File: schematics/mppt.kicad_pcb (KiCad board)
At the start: 2 copper layers, 85.7 x 58.9 mm, 164 parts, among them J1 nokia5110, J2 UART, J3 SWD, J4 buck/boost, J5 HV+, J6 HV-, J7 LV+, J8 LV-, Q1 Q_NMOS_GDS, Q2 Q_NMOS_GDS, SW1 push, SW2 push, SW3 push, SW4 push, SW5 push, U1 LMR16006XDDCR, U2 LMR16006XDDCR, U3 STM32F103C8Tx, U4 INA199, U5 lm5109, U6 INA199

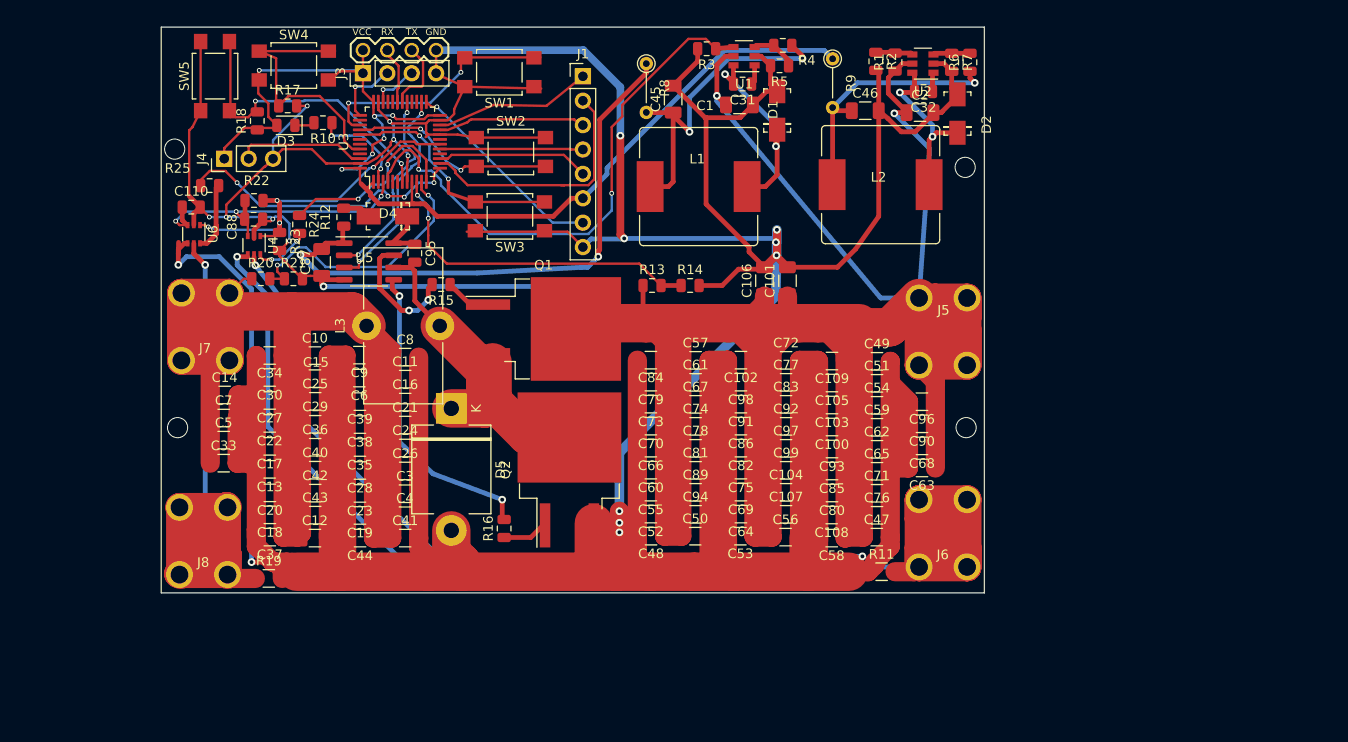
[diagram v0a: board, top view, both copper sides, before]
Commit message: update schematic
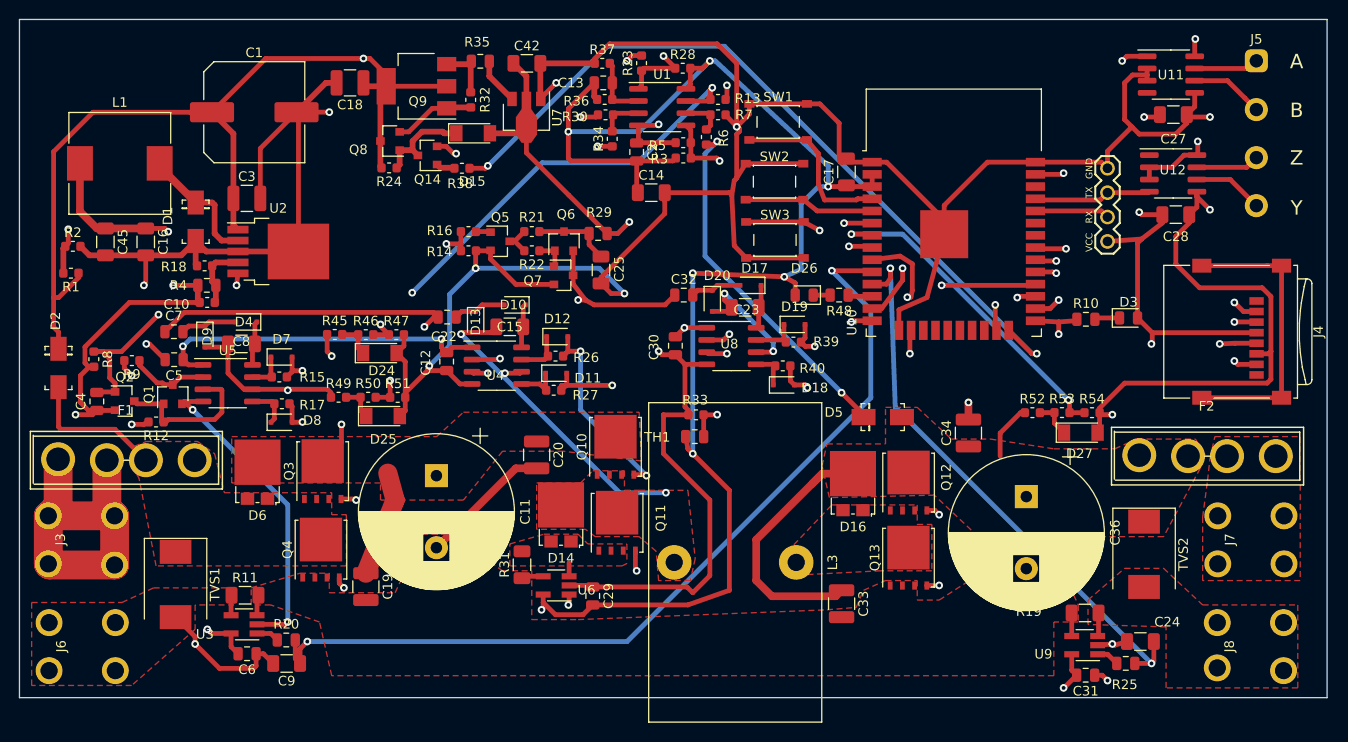
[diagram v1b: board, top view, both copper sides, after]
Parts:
- removed C100, C101, C102, C103, C104, C105, C106, C107, C108, C109, C21, C26, C35, C37, C38, C39, C40, C41, C43, C44, C46, C47, C48, C49, C50, C51, C52, C53, C54, C55, C56, C57, C58, C59, C60, C61, C62, C63, C64, C65, C66, C67, C68, C69, C70, C71, C72, C73, C74, C75, C76, C77, C78, C79, C80, C81, C82, C83, C84, C85, C86, C87, C89, C90, C91, C92, C93, C94, C96, C97, C98, C99: 10uF, Capacitor_SMD:C_1206_3216Metric
- removed C110, C88: .22uF, Capacitor_SMD:C_0805_2012Metric
- removed C95: 1uF, Capacitor_SMD:C_0805_2012Metric
- removed J1: nokia5110, Connector_PinHeader_2.54mm:PinHeader_1x08_P2.54mm_Vertical
- removed L2: 10uH, Inductor_SMD:L_Bourns_SRR1210A
- removed SW4, SW5: push, Button_Switch_SMD:SW_SPST_TL3305A
- added D10: D, Diode_SMD:D_SOD-323F, F.Cu at (149.1, 105.9)
- added D11: D, Diode_SMD:D_SOD-323F, F.Cu at (153.4, 113.0)
- added D12: D, Diode_SMD:D_SOD-323F, F.Cu at (153.5, 109.2)
- added D13: D, Diode_SMD:D_SOD-323F, F.Cu at (145.0, 107.7)
- added D14: D_Schottky_AAK, Package_TO_SOT_SMD:TO-277A, F.Cu at (153.9, 127.8)
- added D15: 5.6v, Diode_SMD:D_MiniMELF, F.Cu at (144.8, 88.1)
- added D16: D_Schottky_AAK, Package_TO_SOT_SMD:TO-277A, F.Cu at (184.3, 124.5)
- added D17: D, Diode_SMD:D_SOD-323F, F.Cu at (173.7, 103.9)
- added D18: D, Diode_SMD:D_SOD-323F, F.Cu at (177.1, 114.3)
- added D19: D, Diode_SMD:D_SOD-323F, F.Cu at (178.2, 108.0)
- added D20: D, Diode_SMD:D_SOD-323F, F.Cu at (169.7, 105.5)
- added D24: 5.6v, Diode_SMD:D_MiniMELF, F.Cu at (135.1, 110.9)
- added D25: 5.6v, Diode_SMD:D_MiniMELF, F.Cu at (135.4, 117.5)
- added D26: YELLOW, LED_SMD:LED_0805_2012Metric, F.Cu at (179.2, 104.9)
- added D27: 5.6v, Diode_SMD:D_MiniMELF, F.Cu at (208.0, 119.2)
- added D6: D_Schottky_AAK, Package_TO_SOT_SMD:TO-277A, F.Cu at (122.3, 123.3)
- added D7: D, Diode_SMD:D_SOD-323F, F.Cu at (124.8, 111.3)
- added D8: D, Diode_SMD:D_SOD-323F, F.Cu at (124.8, 118.1)
- added D9: D, Diode_SMD:D_SOD-323F, F.Cu at (116.8, 109.2)
- added F1: FUSE, mppt_footprints:BladeFuse-CarType, F.Cu at (108.7, 122.1)
- added F2: FUSE, mppt_footprints:BladeFuse-CarType, F.Cu at (221.2, 121.7)
- added Q10: Q_NMOS_GDS, mppt_footprints:TDSON-8-1, F.Cu at (159.6, 120.7)
- added Q11: Q_NMOS_GDS, mppt_footprints:TDSON-8-1, F.Cu at (159.8, 128.6)
- added Q12: Q_NMOS_GDS, mppt_footprints:TDSON-8-1, F.Cu at (190.1, 124.4)
- added Q13: Q_NMOS_GDS, mppt_footprints:TDSON-8-1, F.Cu at (190.1, 132.2)
- added Q14: Q_NPN_BEC, Package_TO_SOT_SMD:SOT-23, F.Cu at (140.0, 90.4)
- added Q3: Q_NMOS_GDS, mppt_footprints:TDSON-8-1, F.Cu at (129.1, 123.2)
- added Q4: Q_NMOS_GDS, mppt_footprints:TDSON-8-1, F.Cu at (128.9, 131.4)
- added Q5: Q_NPN_BEC, Package_TO_SOT_SMD:SOT-23, F.Cu at (147.6, 99.3)
- added Q6: Q_NPN_BEC, Package_TO_SOT_SMD:SOT-23, F.Cu at (154.2, 99.3)
- added Q7: Q_PNP_BCE, Package_TO_SOT_SMD:SOT-23, F.Cu at (154.2, 102.8)
- added Q8: Q_NPN_BEC, Package_TO_SOT_SMD:SOT-23, F.Cu at (136.1, 88.9)
- added Q9: BCP56, Package_TO_SOT_SMD:SOT-223-3_TabPin2, F.Cu at (138.9, 83.2)
- added R26: 33, Resistor_SMD:R_0603_1608Metric, F.Cu at (153.3, 111.3)
- added R27: 33, Resistor_SMD:R_0603_1608Metric, F.Cu at (153.2, 114.8)
- added R28: 10k, Resistor_SMD:R_0603_1608Metric, F.Cu at (166.6, 81.3)
- added R29: 10, Resistor_SMD:R_0805_2012Metric, F.Cu at (157.8, 98.5)
- added R30: 100k, Resistor_SMD:R_0603_1608Metric, F.Cu at (158.6, 86.1)
- added R31: .001, Resistor_SMD:R_1206_3216Metric, F.Cu at (149.9, 133.0)
- added R32: 1k, Resistor_SMD:R_0603_1608Metric, F.Cu at (144.5, 84.6)
- added R33: 10k, Resistor_SMD:R_0603_1608Metric, F.Cu at (168.0, 117.4)
- added R34: 1k, Resistor_SMD:R_0603_1608Metric, F.Cu at (159.3, 88.6)
- added R35: 10, Resistor_SMD:R_0805_2012Metric, F.Cu at (145.5, 80.6)
- added R36: 100k, Resistor_SMD:R_0603_1608Metric, F.Cu at (158.5, 84.5)
- added R37: 10k, Resistor_SMD:R_0603_1608Metric, F.Cu at (158.2, 80.8)
- added R38: 100k, Resistor_SMD:R_0603_1608Metric, F.Cu at (143.6, 91.7)
- added R39: 33, Resistor_SMD:R_0603_1608Metric, F.Cu at (178.1, 109.8)
- added R40: 33, Resistor_SMD:R_0603_1608Metric, F.Cu at (177.0, 112.3)
- added R45: 333k, Resistor_SMD:R_0603_1608Metric, F.Cu at (130.4, 109.0)
- added R46: 10k, Resistor_SMD:R_0603_1608Metric, F.Cu at (133.6, 109.0)
- added R47: 10k, Resistor_SMD:R_0603_1608Metric, F.Cu at (136.8, 109.0)
- added R48: 510, Resistor_SMD:R_0805_2012Metric, F.Cu at (182.9, 104.9)
- added R49: 333k, Resistor_SMD:R_0603_1608Metric, F.Cu at (130.8, 115.5)
- added R50: 10k, Resistor_SMD:R_0603_1608Metric, F.Cu at (133.8, 115.5)
- added R51: 10k, Resistor_SMD:R_0603_1608Metric, F.Cu at (136.9, 115.5)
- added R52: 333k, Resistor_SMD:R_0603_1608Metric, F.Cu at (203.0, 117.1)
- added R53: 10k, Resistor_SMD:R_0603_1608Metric, F.Cu at (206.1, 117.1)
- added R54: 10k, Resistor_SMD:R_0603_1608Metric, F.Cu at (209.2, 117.1)
- added TH1: Thermistor_NTC, Resistor_SMD:R_0805_2012Metric, F.Cu at (167.8, 119.6)
- added TVS1: TVS, Diode_SMD:D_SMC, F.Cu at (113.8, 135.0)
- added TVS2: TVS, Diode_SMD:D_SMC, F.Cu at (214.6, 131.9)
- added U10: ESP32-WROOM-32D, RF_Module:ESP32-WROOM-32, F.Cu at (194.8, 99.3)
- added U11: ST485EBDR, Package_SO:SOIC-8_3.9x4.9mm_P1.27mm, F.Cu at (217.4, 81.9)
- added U12: ST485EBDR, Package_SO:SOIC-8_3.9x4.9mm_P1.27mm, F.Cu at (217.7, 92.2)
- added U7: AMS1117-5.0, Package_TO_SOT_SMD:SOT-89-3, F.Cu at (150.3, 86.0)
- added U8: lm5109, Package_SO:SO-8_3.9x4.9mm_P1.27mm, F.Cu at (171.7, 110.2)
- added U9: INA180, Package_TO_SOT_SMD:SOT-23-5_HandSoldering, F.Cu at (208.4, 141.3)
- C1: value 10uF -> 33uF 100v; footprint Capacitor_SMD:C_1206_3216Metric -> Capacitor_SMD:C_Elec_10x10.2
- C10: value 10uF -> 33nF; footprint Capacitor_SMD:C_1206_3216Metric -> Capacitor_SMD:C_0603_1608Metric
- C11, C36: value 10uF -> 470uF; footprint Capacitor_SMD:C_1206_3216Metric -> Capacitor_THT:CP_Radial_D16.0mm_P7.50mm
- C12, C30, C4, C5: footprint Capacitor_SMD:C_1206_3216Metric -> Capacitor_SMD:C_0805_2012Metric
- C13, C2, C22, C6, C7: value 10uF -> 100nF; footprint Capacitor_SMD:C_1206_3216Metric -> Capacitor_SMD:C_0805_2012Metric
- C15, C23, C24, C27, C28, C42, C8, C9: value 10uF -> 1uF
- C18, C3: value 10uF -> 4.7uF; footprint Capacitor_SMD:C_1206_3216Metric -> Capacitor_SMD:C_1210_3225Metric
- C19, C20, C33, C34: value 10uF -> 4.7uF 100v; footprint Capacitor_SMD:C_1206_3216Metric -> Capacitor_SMD:C_1210_3225Metric
- C29: value 10uF -> 1uF; footprint Capacitor_SMD:C_1206_3216Metric -> Capacitor_SMD:C_0805_2012Metric
- C31: value .22uF -> 1uF
- C32: value .22uF -> 100nF
- D3: value RED -> GREEN
- D4: footprint mppt_footprints:DO-214AC -> Diode_SMD:D_SOD-323F
- D5: footprint Diode_THT:D_5KPW_P12.70mm_Horizontal -> mppt_footprints:DO-214AC
- J2: footprint hbridge_footprints:uart -> mppt_footprints:uart
- J3: value SWD -> IN+; footprint Connector_PinHeader_2.54mm:PinHeader_1x04_P2.54mm_Vertical -> mppt_footprints:screw_terminal
- J4: value buck/boost -> Micro_SD_Card; footprint Connector_PinHeader_2.54mm:PinHeader_1x03_P2.54mm_Vertical -> Connector_Card:microSD_HC_Wuerth_693072010801
- J5: value HV+ -> Conn_01x04; footprint hbridge_footprints:screw_terminal -> mppt_footprints:rs422connector
- J6: value HV- -> IN-; footprint hbridge_footprints:screw_terminal -> mppt_footprints:screw_terminal
- J7: value LV+ -> OUT+; footprint hbridge_footprints:screw_terminal -> mppt_footprints:screw_terminal
- J8: value LV- -> OUT-; footprint hbridge_footprints:screw_terminal -> mppt_footprints:screw_terminal
- L1: value 10uH -> 100uH; footprint Inductor_SMD:L_Bourns_SRR1210A -> Inductor_SMD:L_10.4x10.4_H4.8
- L3: footprint Inductor_THT:L_Toroid_Vertical_L16.0mm_W8.0mm_P7.62mm -> Inductor_THT:L_Toroid_Vertical_L33.0mm_W17.8mm_P12.70mm_Pulse_KM-5
- Q1: footprint Package_TO_SOT_SMD:TO-263-2 -> Package_TO_SOT_SMD:SOT-23
- Q2: value Q_NMOS_GDS -> Q_PMOS_GSD; footprint Package_TO_SOT_SMD:TO-263-2 -> Package_TO_SOT_SMD:SOT-23
- R1, R14, R15, R18, R2, R21, R22, R5: footprint Resistor_SMD:R_0805_2012Metric -> Resistor_SMD:R_0603_1608Metric
- R12: value 2.2 -> 200k; footprint Resistor_SMD:R_0805_2012Metric -> Resistor_SMD:R_0603_1608Metric
- R13: value 120k -> 100k; footprint Resistor_SMD:R_0805_2012Metric -> Resistor_SMD:R_0603_1608Metric
- R16: value 33 -> 10k; footprint Resistor_SMD:R_0805_2012Metric -> Resistor_SMD:R_0603_1608Metric
- R17: value 10k -> 33; footprint Resistor_SMD:R_0805_2012Metric -> Resistor_SMD:R_0603_1608Metric
- R20: value 120k -> 510
- R23: value 10k -> 200k; footprint Resistor_SMD:R_0805_2012Metric -> Resistor_SMD:R_0603_1608Metric
- R24: value 510 -> 100k; footprint Resistor_SMD:R_0805_2012Metric -> Resistor_SMD:R_0603_1608Metric
- R3: value 120k -> 10k; footprint Resistor_SMD:R_0805_2012Metric -> Resistor_SMD:R_0603_1608Metric
- R6: value 33k -> 47k; footprint Resistor_SMD:R_0805_2012Metric -> Resistor_SMD:R_0603_1608Metric
- R7: value 10k -> 1k; footprint Resistor_SMD:R_0805_2012Metric -> Resistor_SMD:R_0603_1608Metric
- R8, R9: value 0 -> 200k; footprint Resistor_THT:R_Axial_DIN0204_L3.6mm_D1.6mm_P5.08mm_Vertical -> Resistor_SMD:R_0603_1608Metric
- SW1: value push -> page; footprint Button_Switch_SMD:SW_SPST_TL3305A -> mppt_footprints:SW_SPST_PTS810
- SW2: value push -> menu; footprint Button_Switch_SMD:SW_SPST_TL3305A -> mppt_footprints:SW_SPST_PTS810
- SW3: value push -> boot; footprint Button_Switch_SMD:SW_SPST_TL3305A -> mppt_footprints:SW_SPST_PTS810
- U1: value LMR16006XDDCR -> LM393; footprint Package_TO_SOT_SMD:SOT-23-6 -> Package_SO:SOIC-8_3.9x4.9mm_P1.27mm
- U2: value LMR16006XDDCR -> APE1707H-33-HF; footprint Package_TO_SOT_SMD:SOT-23-6 -> Package_TO_SOT_SMD:TO-252-5_TabPin3
- U3: value STM32F103C8Tx -> INA180; footprint Package_QFP:LQFP-48_7x7mm_P0.5mm -> Package_TO_SOT_SMD:SOT-23-5_HandSoldering
- U4: value INA199 -> lm5109; footprint Package_TO_SOT_SMD:SOT-363_SC-70-6 -> Package_SO:SO-8_3.9x4.9mm_P1.27mm
- U6: value INA199 -> INA180; footprint Package_TO_SOT_SMD:SOT-363_SC-70-6 -> Package_TO_SOT_SMD:SOT-23-5_HandSoldering
- moved R25 107.6 mm to (212.7, 143.2), turned to 0 degrees
- moved J4 107.5 mm to (224.8, 108.7), turned to 270 degrees
- moved J7 105.1 mm to (222.3, 132.9), turned to 90 degrees
- moved J8 103.5 mm to (222.2, 144.0), turned to 90 degrees
- moved C27 98.7 mm to (217.7, 86.1), turned to 0 degrees
- moved D2 97.3 mm to (101.6, 112.5), turned to 270 degrees
- moved J6 96.2 mm to (100.6, 144.0), turned to 90 degrees
- moved D3 90.0 mm to (213.0, 107.3), turned to 0 degrees
- moved C28 89.0 mm to (217.9, 96.5), turned to 0 degrees
- moved R1 88.6 mm to (102.9, 102.6), turned to 180 degrees
- moved R2 85.8 mm to (103.1, 99.8), turned to 0 degrees
- moved R19 85.1 mm to (208.5, 138.0), turned to 180 degrees
- moved R10 82.0 mm to (208.6, 107.4), turned to 0 degrees
- moved J2 80.0 mm to (210.8, 99.3), turned to 90 degrees
- moved R9 79.4 mm to (109.2, 111.7), turned to 180 degrees
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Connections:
- C1 pad 1: VCC -> Net-(C1-Pad1)
- C10 pad 1: VDD -> +3V3
- C10 pad 2: GND -> Net-(C10-Pad2)
- C11 pad 2: GND -> Net-(C11-Pad2)
- C12 pad 1: VDD -> +12V
- C13 pad 1: VDD -> Net-(C13-Pad1)
- C13 pad 2: GND -> +3V3
- C14 pad 1: VDD -> +3V3
- C15 pad 1: VDD -> Net-(C15-Pad1)
- C15 pad 2: GND -> Net-(C15-Pad2)
- C16 pad 1: VDD -> +3V3
- C17 pad 1: VDD -> +3V3
- C18 pad 1: VDD -> Net-(C1-Pad1)
- C19 pad 2: GND -> Net-(C11-Pad2)
- C2 pad 1: VCC -> GND
- C2 pad 2: GND -> +3V3
- C20 pad 2: GND -> Net-(C11-Pad2)
- C22 pad 1: VDD -> Net-(C22-Pad1)
- C22 pad 2: GND -> Net-(C22-Pad2)
- C23 pad 1: VDD -> Net-(C23-Pad1)
- C23 pad 2: GND -> Net-(C23-Pad2)
- C24 pad 1: VDD -> LC
- C25 pad 1: VDD -> GND
- C25 pad 2: GND -> Net-(C25-Pad2)
- C27 pad 1: VDD -> +3V3
- C28 pad 1: VDD -> +3V3
- C29 pad 1: VDD -> GND
- C29 pad 2: GND -> +3V3
- C3 pad 1: VDD -> Net-(C1-Pad1)
- C30 pad 1: VDD -> +12V
- C31 pad 1: Net-(C31-Pad1) -> GND
- C31 pad 2: Net-(C31-Pad2) -> +3V3
- C32 pad 1: Net-(C32-Pad1) -> Net-(C22-Pad1)
- C33 pad 1: VDD -> VCC
- C33 pad 2: GND -> Net-(C11-Pad2)
- C34 pad 1: VDD -> VCC
- C34 pad 2: GND -> Net-(C11-Pad2)
- C36 pad 1: VDD -> VCC
- C36 pad 2: GND -> Net-(C11-Pad2)
- C4 pad 1: VDD -> +3V3
- C4 pad 2: GND -> Net-(C4-Pad2)
- C42 pad 1: VDD -> +12V
- C45 pad 1: Net-(C45-Pad1) -> +3V3
- C5 pad 1: VDD -> +12V
- C6 pad 1: VDD -> GND
- C6 pad 2: GND -> +3V3
- C7 pad 1: VDD -> Net-(C22-Pad1)
- C7 pad 2: GND -> Net-(C7-Pad2)
- C8 pad 1: VDD -> VEE
- C8 pad 2: GND -> Net-(C8-Pad2)
- C9 pad 1: VDD -> HC
- D1 pad 1: Net-(C31-Pad2) -> Net-(D1-Pad1)
- D2 pad 1: Net-(C32-Pad2) -> Net-(C1-Pad1)
- D2 pad 2: GND -> VEE
- D4 pad 1: Net-(C95-Pad1) -> Net-(C8-Pad2)
- D4 pad 2: Net-(D4-Pad2) -> Net-(C7-Pad2)
- D5 pad 1: Net-(C95-Pad2) -> Net-(C1-Pad1)
- D5 pad 2: GND -> VCC
- J3 pad 1: +3V3 -> Net-(F1-Pad1)
- J4 pad 1: +3V3 -> Net-(J4-Pad1)
- J4 pad 3: GND -> Net-(J4-Pad3)
- J5 pad 1: VCC -> Net-(J5-Pad1)
- J6 pad 1: Net-(J6-Pad1) -> GND
- J7 pad 1: VDD -> Net-(F2-Pad2)
- L1 pad 1: Net-(C45-Pad1) -> +3V3
- L1 pad 2: Net-(C31-Pad2) -> Net-(D1-Pad1)
- L3 pad 1: VDD -> Net-(C23-Pad1)
- L3 pad 2: Net-(C95-Pad2) -> Net-(C15-Pad1)
- Q1 pad 2: VCC -> GND
- Q1 pad 3: Net-(C95-Pad2) -> Net-(Q1-Pad3)
- Q2 pad 1: Net-(Q2-Pad1) -> Net-(C4-Pad2)
- Q2 pad 2: Net-(C95-Pad2) -> +3V3
- Q2 pad 3: GND -> Net-(Q1-Pad1)
- R1 pad 1: VCC -> Net-(C1-Pad1)
- R11 pad 2: Net-(J6-Pad1) -> Net-(C11-Pad2)
- R12 pad 1: Net-(D4-Pad2) -> Net-(Q1-Pad1)
- R12 pad 2: +12V -> PWR_L
- R13 pad 1: VCC -> Net-(C4-Pad2)
- R13 pad 2: HV -> Net-(R13-Pad2)
- R14 pad 1: HV -> CHARGE_PUMP
- R15 pad 1: Net-(Q1-Pad1) -> Net-(D7-Pad2)
- R16 pad 1: Net-(Q2-Pad1) -> Net-(Q5-Pad1)
- R16 pad 2: Net-(R16-Pad2) -> CHARGE_PUMP
- R17 pad 1: boot0 -> Net-(D8-Pad2)
- R17 pad 2: GND -> Net-(D8-Pad1)
- R18 pad 1: +3V3 -> Net-(C10-Pad2)
- R18 pad 2: reset -> GND
- R19 pad 2: GND -> Net-(C11-Pad2)
- R20 pad 1: VDD -> Net-(R20-Pad1)
- R20 pad 2: LV -> HC
- R21 pad 1: LV -> Net-(C25-Pad2)
- R21 pad 2: GND -> Net-(Q5-Pad3)
- R22 pad 1: AMP -> Net-(Q6-Pad1)
- R22 pad 2: CSREF -> Net-(Q5-Pad3)
- R23 pad 1: CSREF -> Net-(R23-Pad1)
- R23 pad 2: GND -> BUCK_L
- R24 pad 1: Net-(R24-Pad1) -> Net-(D15-Pad1)
- R24 pad 2: HC -> Net-(C1-Pad1)
- R3 pad 1: PWRDN -> +3V3
- R3 pad 2: GND -> Net-(R13-Pad2)
- R4 pad 1: Net-(C45-Pad1) -> +3V3
- R4 pad 2: Net-(R4-Pad2) -> Net-(C10-Pad2)
- R5 pad 1: Net-(R4-Pad2) -> Net-(R13-Pad2)
- R6 pad 1: Net-(C46-Pad1) -> Net-(C1-Pad1)
- R8 pad 1: +12V -> Net-(C4-Pad2)
- R8 pad 2: Net-(C45-Pad1) -> +3V3
- R9 pad 1: +3V3 -> Net-(Q1-Pad3)
- R9 pad 2: Net-(C46-Pad1) -> PWR_H
- SW1 pad 2: sw1 -> Net-(SW1-Pad2)
- SW2 pad 2: sw2 -> Net-(SW2-Pad2)
- SW3 pad 1: GND -> Net-(R10-Pad1)
- SW3 pad 2: sw3 -> GND
- U1 pad 1: Net-(C31-Pad1) -> Net-(R23-Pad1)
- U1 pad 2: GND -> Net-(C13-Pad1)
- U1 pad 3: Net-(R4-Pad2) -> Net-(R30-Pad1)
- U1 pad 4: PWRDN -> GND
- U1 pad 5: VCC -> Net-(R13-Pad2)
- U1 pad 6: Net-(C31-Pad2) -> Net-(R6-Pad2)
- U2 pad 1: Net-(C32-Pad1) -> Net-(C1-Pad1)
- U2 pad 2: GND -> Net-(D1-Pad1)
- U2 pad 3: Net-(R6-Pad2) -> GND
- U2 pad 4: Net-(R1-Pad2) -> Net-(C10-Pad2)
- U2 pad 5: VCC -> Net-(R1-Pad2)
- U3 pad 1: +3V3 -> Net-(R20-Pad1)
- U3 pad 2: Net-(R10-Pad1) -> GND
- U3 pad 3: AMP -> Net-(C11-Pad2)
- U3 pad 4: PWRDN -> GND
- U3 pad 5: Net-(U3-Pad5) -> +3V3
- U4 pad 1: CSREF -> +12V
- U4 pad 2: GND -> BUCK_H
- U4 pad 3: AMP -> BUCK_L
- U4 pad 4: Net-(J6-Pad1) -> GND
- U4 pad 5: GND -> Net-(D11-Pad1)
- U4 pad 6: Net-(R24-Pad1) -> Net-(C15-Pad1)
- U5 pad 2: Net-(U3-Pad29) -> Net-(Q1-Pad3)
- U5 pad 3: Net-(U3-Pad26) -> Net-(Q1-Pad1)
- U5 pad 5: Net-(R16-Pad2) -> Net-(D8-Pad1)
- U5 pad 6: Net-(C95-Pad2) -> VEE
- U5 pad 8: Net-(C95-Pad1) -> Net-(C8-Pad2)
- U6 pad 1: CSREF -> Net-(R34-Pad1)
- U6 pad 3: AMP -> Net-(D14-Pad1)
- U6 pad 4: GND -> Net-(C11-Pad2)
- U6 pad 5: Net-(J8-Pad1) -> +3V3
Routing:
- net +3V3: track 118.4 -> 450.5 mm, vias 6 -> 17
- net VCC: track 328.2 -> 34.3 mm, vias 2 -> 0
- net GND: track 842.6 -> 589.2 mm, vias 21 -> 19
- net Net-(C1-Pad1): track 0.00 -> 183.7 mm, vias 0 -> 3
- net Net-(J6-Pad1): track 147.9 -> 0.00 mm, vias 1 -> 0
- net VDD: track 172.3 -> 25.7 mm, vias 0 -> 2
- net PWR_H: track 0.00 -> 104.6 mm, vias 0 -> 2
- net PWR_L: track 0.00 -> 102.3 mm, vias 0 -> 2
- net BUCK_L: track 0.00 -> 91.7 mm, vias 0 -> 3
- net Net-(C4-Pad2): track 0.00 -> 85.7 mm, vias 0 -> 3
- net BUCK_H: track 0.00 -> 82.2 mm, vias 0 -> 2
- net PWRDWN: track 0.00 -> 81.5 mm, vias 0 -> 2
- net Net-(J8-Pad1): track 83.1 -> 2.44 mm, vias 1 -> 0
- net HC: track 20.2 -> 93.6 mm
- net CHARGE_PUMP: track 0.00 -> 72.6 mm, vias 0 -> 2
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- added copper zone on F.Cu, net GND
- added copper zone on F.Cu, net Net-(C11-Pad2)
- added copper zone on F.Cu, net Net-(C15-Pad1)
- added copper zone on F.Cu, net Net-(C23-Pad1)
- added copper zone on F.Cu, net Net-(D14-Pad1)
- added copper zone on F.Cu, net Net-(F2-Pad2)
- added copper zone on F.Cu, net Net-(J8-Pad1)
- added copper zone on F.Cu, net VCC
- added copper zone on F.Cu, net VDD
- added copper zone on F.Cu, net VEE
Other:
- board size 85.7 x 58.9 mm -> 136.1 x 70.6 mm
- copper layers 2 -> 4
